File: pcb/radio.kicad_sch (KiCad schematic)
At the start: 0 parts

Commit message: feat: added documentation, updated page information
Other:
- title: Banshee Power Delivery System -> Banshee Long Range Radio
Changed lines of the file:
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@@
 	(paper "A4")
 	(title_block
-		(title "Banshee Power Delivery System")
+		(title "Banshee Long Range Radio")
 		(date "2026-02-26")
 		(rev "1")

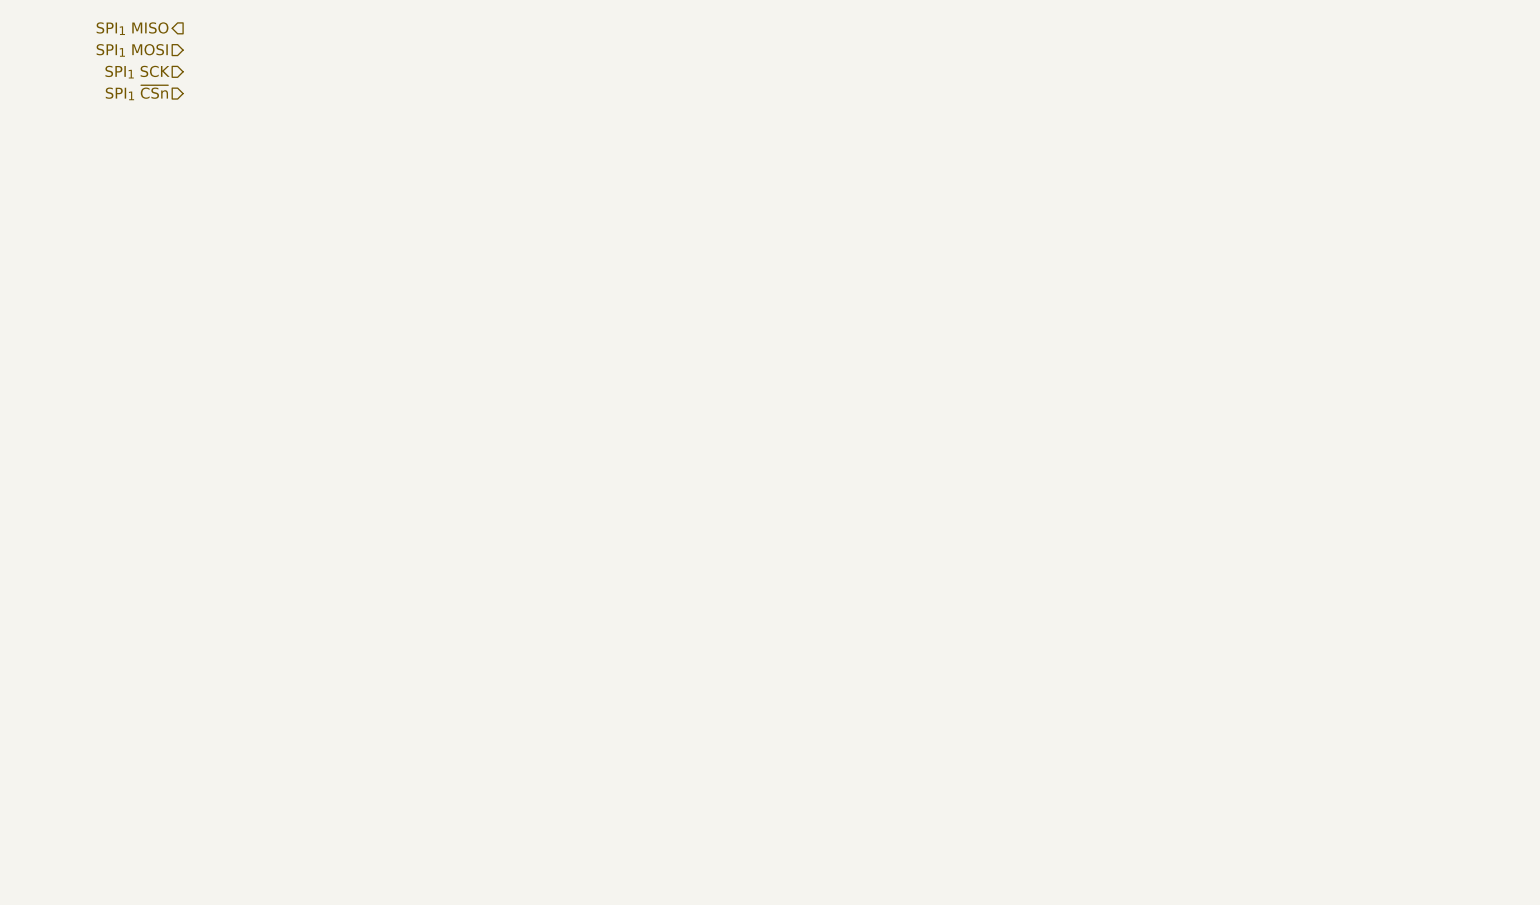
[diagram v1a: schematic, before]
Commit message: feat: sx1278 radio
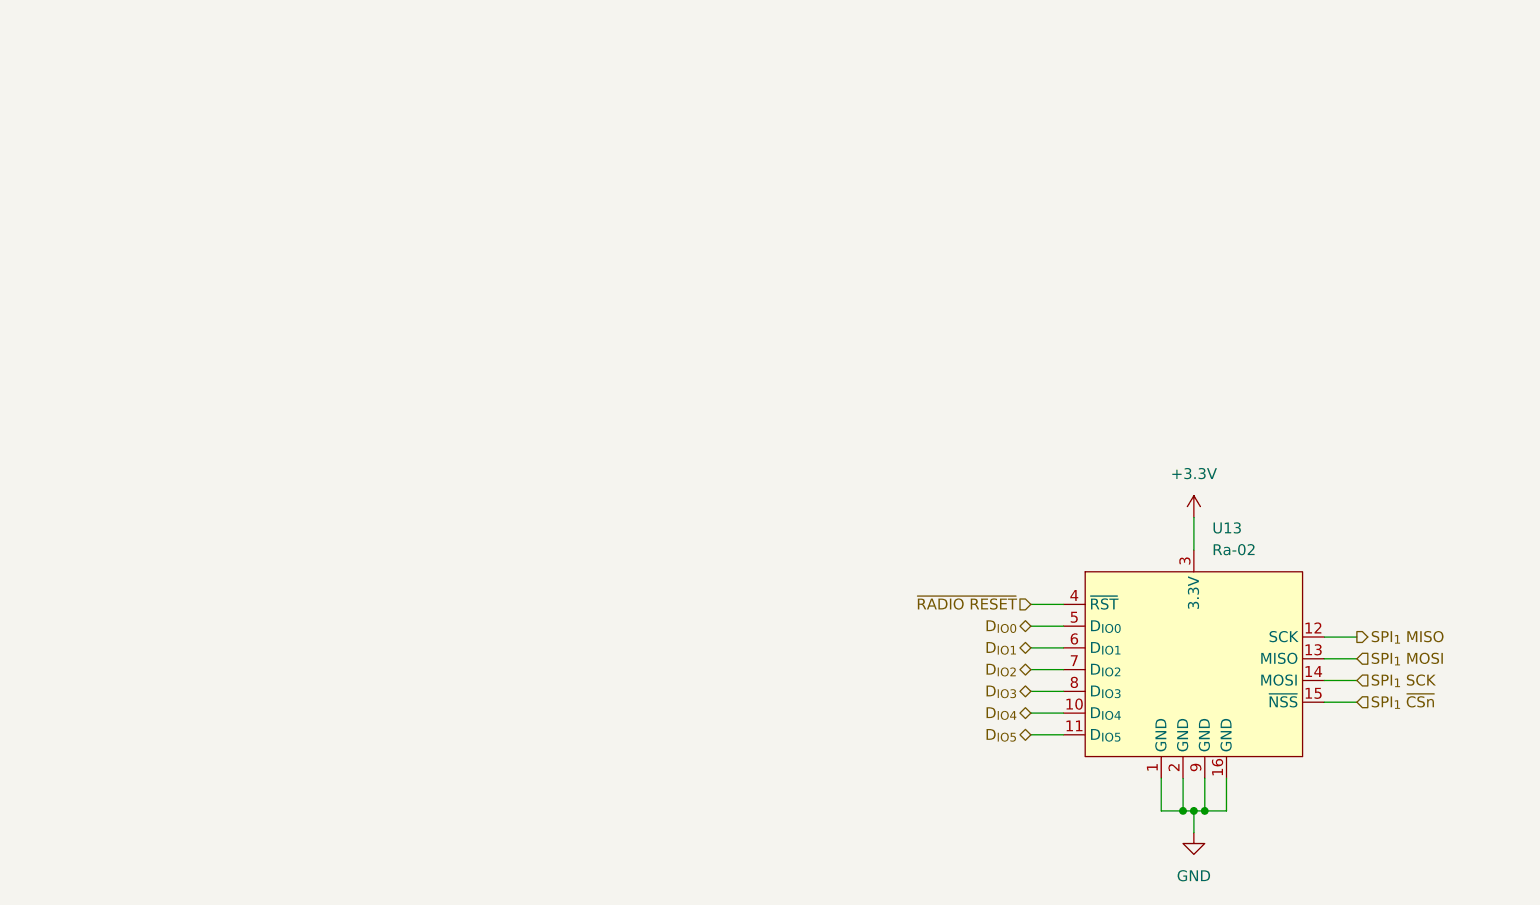
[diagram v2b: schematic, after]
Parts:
- added U13: Ra-02, symbol Banshee:Ra-02
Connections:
- net SPI_{1} MISO: now also U13.12 (SCK)
- net SPI_{1} MOSI: now also U13.13 (MISO)
- net SPI_{1} SCK: now also U13.14 (MOSI)
- net SPI_{1} ~{CSn}: now also U13.15 (~{NSS})
- new net +3.3V: U13.3 (3.3V)
- new net D_{IO0}: U13.5 (D_{IO0})
- new net D_{IO1}: U13.6 (D_{IO1})
- new net D_{IO2}: U13.7 (D_{IO2})
- new net D_{IO3}: U13.8 (D_{IO3})
- new net D_{IO4}: U13.10 (D_{IO4})
- new net D_{IO5}: U13.11 (D_{IO5})
- new net GND: U13.1 (GND), U13.16 (GND), U13.2 (GND), U13.9 (GND)
- new net ~{RADIO RESET}: U13.4 (~{RST})

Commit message: feat: set pcbnew settings
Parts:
- U13: now left out of the parts list
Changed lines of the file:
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@@
 		(unit 1)
 		(exclude_from_sim no)
-		(in_bom yes)
+		(in_bom no)
 		(on_board yes)
 		(dnp no)
